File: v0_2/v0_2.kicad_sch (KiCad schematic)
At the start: 1 part, among them IC1 RASPBERRY_PI_PICO_W

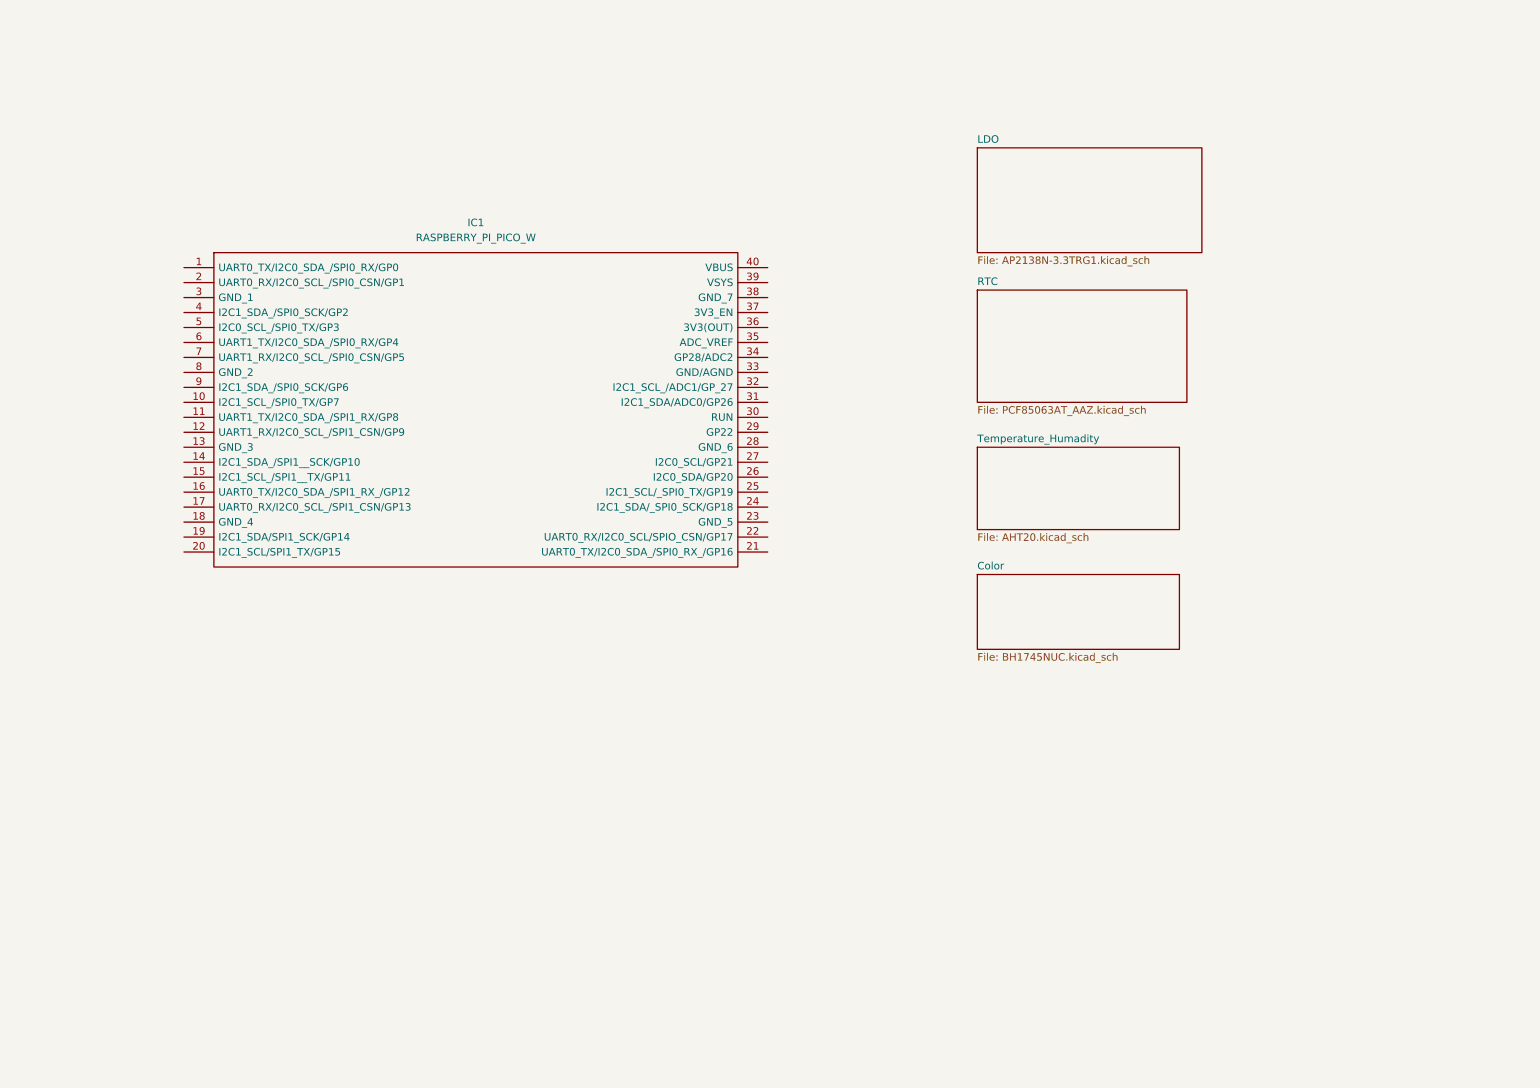
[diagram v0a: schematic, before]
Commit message: add sensor schematic
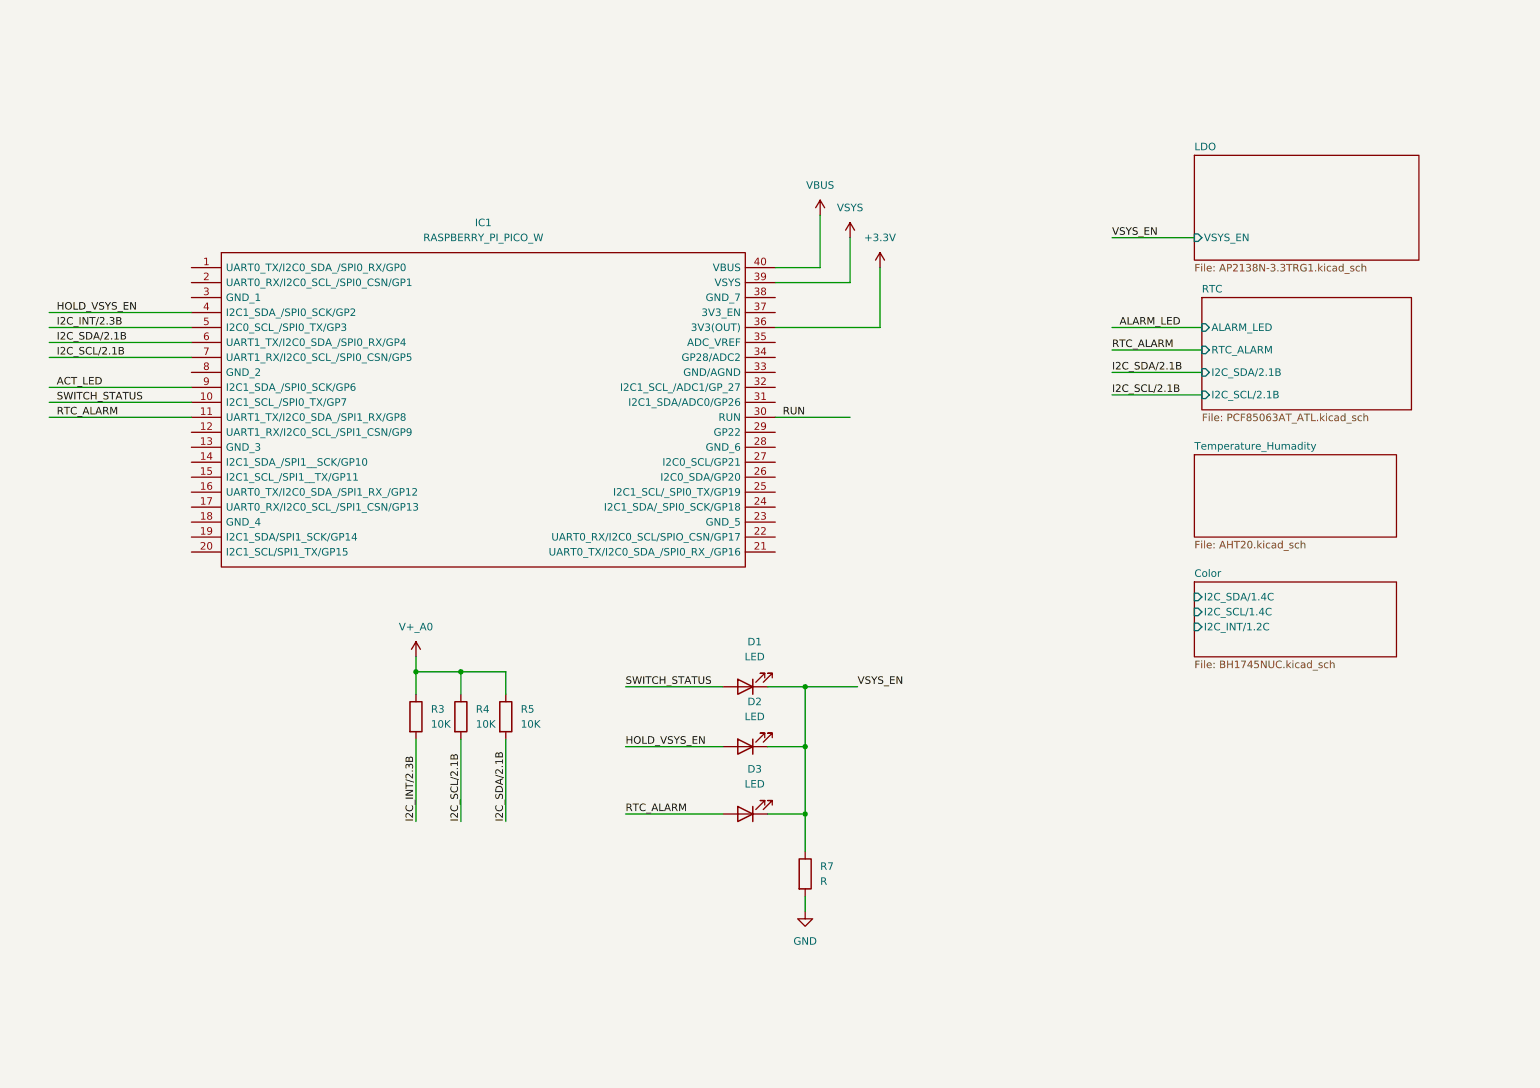
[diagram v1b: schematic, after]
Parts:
- added D1, D2, D3: LED, symbol Device:LED
- added R3, R4, R5: 10K, symbol Device:R
- added R7: R, symbol Device:R
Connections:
- net SWITCH_STATUS: now reaches IC1.10 (I2C1_SCL_/SPI0_TX/GP7)
- net SWITCH_STATUS: now also D1.2 (A)
- net RTC_ALARM: now reaches IC1.11 (UART1_TX/I2C0_SDA_/SPI1_RX/GP8)
- net RTC_ALARM: now also D3.2 (A)
- net RUN: now reaches IC1.30 (RUN)
- net +3.3V: now reaches IC1.36 (3V3(OUT))
- net VSYS: now reaches IC1.39 (VSYS)
- net HOLD_VSYS_EN: now reaches IC1.4 (I2C1_SDA_/SPI0_SCK/GP2)
- net HOLD_VSYS_EN: now also D2.2 (A)
- net VBUS: now reaches IC1.40 (VBUS)
- net I2C_INT/2.3B: now reaches IC1.5 (I2C0_SCL_/SPI0_TX/GP3)
- net I2C_INT/2.3B: now also R3.2
- net I2C_SDA/2.1B: now reaches IC1.6 (UART1_TX/I2C0_SDA_/SPI0_RX/GP4)
- net I2C_SDA/2.1B: now also R5.2
- net I2C_SCL/2.1B: now reaches IC1.7 (UART1_RX/I2C0_SCL_/SPI0_CSN/GP5)
- net I2C_SCL/2.1B: now also R4.2
- net ACT_LED: now reaches IC1.9 (I2C1_SDA_/SPI0_SCK/GP6)
- new net GND: R7.2
- new net V+_A0: R3.1, R4.1, R5.1
- new net VSYS_EN: D1.1 (K), D2.1 (K), D3.1 (K), R7.1
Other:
- sheet Color ports: added I2C_INT/1.2C, I2C_SCL/1.4C, I2C_SDA/1.4C; removed none
- sheet LDO ports: added VSYS_EN; removed none
- sheet RTC: file PCF85063AT_AAZ.kicad_sch -> PCF85063AT_ATL.kicad_sch
- sheet RTC ports: added ALARM_LED, I2C_SCL/2.1B, I2C_SDA/2.1B, RTC_ALARM; removed none
- moved on the sheet: IC1

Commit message: add color sensor
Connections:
- net RESET: now reaches IC1.12 (UART1_RX/I2C0_SCL_/SPI1_CSN/GP9)
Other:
- sheet Color: file BH1745NUC.kicad_sch -> BH1750FVI.kicad_sch
- sheet Color ports: added RESET; removed I2C_INT/1.2C
- sheet Temperature_Humadity ports: added I2C_SCL, I2C_SDA; removed none
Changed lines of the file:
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@@
+    (stroke (width 0) (type default))
+  )
+  (wire (pts (xy 204.47 115.57) (xy 218.44 115.57))
     (stroke (width 0) (type default))
   )
@@
     (stroke (width 0) (type default))
   )
+  (wire (pts (xy 204.47 99.06) (xy 218.44 99.06))
+    (stroke (width 0) (type default))
+  )
   (wire (pts (xy 121.92 140.97) (xy 138.43 140.97))
     (stroke (width 0) (type default))
@@
     (stroke (width 0) (type default))
   )
+  (wire (pts (xy 204.47 120.65) (xy 218.44 120.65))
+    (stroke (width 0) (type default))
+  )
   (wire (pts (xy 204.47 73.66) (xy 219.71 73.66))
     (stroke (width 0) (type default))
@@
     (stroke (width 0) (type default))
   )
+  (wire (pts (xy 204.47 96.52) (xy 218.44 96.52))
+    (stroke (width 0) (type default))
+  )
   (wire (pts (xy 147.32 69.85) (xy 165.1 69.85))
     (stroke (width 0) (type default))
@@
     (stroke (width 0) (type default))
   )
+  (wire (pts (xy 24.13 87.63) (xy 48.26 87.63))
+    (stroke (width 0) (type default))
+  )
   (wire (pts (xy 93.98 139.7) (xy 93.98 153.67))
     (stroke (width 0) (type default))
@@
     (stroke (width 0) (type default))
   )
+  (wire (pts (xy 204.47 118.11) (xy 218.44 118.11))
+    (stroke (width 0) (type default))
+  )
   (wire (pts (xy 165.1 69.85) (xy 165.1 59.69))
     (stroke (width 0) (type default))
@@
     (effects (font (size 1.27 1.27)) (justify left bottom))
   )
+  (label "I2C_SDA{slash}2.1B" (at 204.47 118.11 0) (fields_autoplaced)
+    (effects (font (size 1.27 1.27)) (justify left bottom))
+  )
+  (label "RESET" (at 25.4 87.63 0) (fields_autoplaced)
+    (effects (font (size 1.27 1.27)) (justify left bottom))
+  )
+  (label "RESET" (at 204.47 115.57 0) (fields_autoplaced)
+    (effects (font (size 1.27 1.27)) (justify left bottom))
+  )
   (label "HOLD_VSYS_EN" (at 25.4 67.31 0) (fields_autoplaced)
     (effects (font (size 1.27 1.27)) (justify left bottom))
@@
     (effects (font (size 1.27 1.27)) (justify left bottom))
   )
+  (label "I2C_SDA{slash}2.1B" (at 204.47 96.52 0) (fields_autoplaced)
+    (effects (font (size 1.27 1.27)) (justify left bottom))
+  )
+  (label "I2C_SCL{slash}2.1B" (at 204.47 99.06 0) (fields_autoplaced)
+    (effects (font (size 1.27 1.27)) (justify left bottom))
+  )
   (label "I2C_SCL{slash}2.1B" (at 204.47 81.28 0) (fields_autoplaced)
     (effects (font (size 1.27 1.27)) (justify left bottom))
@@
   )
   (label "I2C_INT{slash}2.3B" (at 25.4 69.85 0) (fields_autoplaced)
+    (effects (font (size 1.27 1.27)) (justify left bottom))
+  )
+  (label "I2C_SCL{slash}2.1B" (at 204.47 120.65 0) (fields_autoplaced)
     (effects (font (size 1.27 1.27)) (justify left bottom))
   )
@@
       (effects (font (size 1.27 1.27)) (justify left bottom))
     )
-    (property "Sheetfile" "BH1745NUC.kicad_sch" (at 218.44 126.3146 0)
+    (property "Sheetfile" "BH1750FVI.kicad_sch" (at 218.44 126.3146 0)
       (effects (font (size 1.27 1.27)) (justify left top))
     )
-    (pin "I2C_SDA{slash}1.4C" input (at 218.44 115.57 180)
-      (effects (font (size 1.27 1.27)) (justify left))
-    )
-    (pin "I2C_SCL{slash}1.4C" input (at 218.44 118.11 180)
-      (effects (font (size 1.27 1.27)) (justify left))
-    )
-    (pin "I2C_INT{slash}1.2C" input (at 218.44 120.65 180)
+    (pin "RESET" input (at 218.44 115.57 180)
+      (effects (font (size 1.27 1.27)) (justify left))
+    )
+    (pin "I2C_SDA{slash}1.4C" input (at 218.44 118.11 180)
+      (effects (font (size 1.27 1.27)) (justify left))
+    )
+    (pin "I2C_SCL{slash}1.4C" input (at 218.44 120.65 180)
       (effects (font (size 1.27 1.27)) (justify left))
     )
@@
       (effects (font (size 1.27 1.27)) (justify left top))
     )
-    (instances
+    (pin "I2C_SDA" input (at 218.44 96.52 180)
+      (effects (font (size 1.27 1.27)) (justify left))
+    )
+    (pin "I2C_SCL" input (at 218.44 99.06 180)
+      (effects (font (size 1.27 1.27)) (justify left))
+    )
+    (instances

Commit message: schematic for enviro done
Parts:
- removed D3: LED, symbol Device:LED
- added D3: 1PS88SB48, Package_TO_SOT_SMD:SOT-363_SC-70-6, symbol PCM_Diode_Schottky_AKL:1PS88SB48
- added R15, R16: R, symbol Device:R
- added S1, S2: TS-1101-C-W, TS-1101-C-W:TS1101CW, symbol TS-1101-C-W:TS-1101-C-W
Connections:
- net +3.3V: now also R3.1, R4.1, R5.1
- net ACT_LED: now also R7.1
- net ALARM_LED: now also R15.1
- net GND: now also D1.1 (K), D2.1 (K), R16.2, S1.2 (NO); no longer R7.2
- net HOLD_VSYS_EN: now also D3.4 (A2); no longer D2.2 (A)
- net RTC_ALARM: now also D3.5 (A2)
- net RUN: now also S1.1 (COM)
- net SWITCH_STATUS: now also D3.1 (A1), S2.1 (COM); no longer D1.2 (A)
- net V+_A0: now also S2.2 (NO); no longer R3.1, R4.1, R5.1
- net VSYS_EN: now also D3.3 (K2), D3.6 (K1), R16.1; no longer D1.1 (K), D2.1 (K), R7.1
- new net: D2.2 (A), R15.2
- new net: D1.2 (A), R7.2
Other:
- sheet LDO ports: added V+_A0; removed none
- sheet RTC ports: added V+_A0; removed none
- note added: "User Interface"
- moved on the sheet: D1, D2, R3, R4, R5

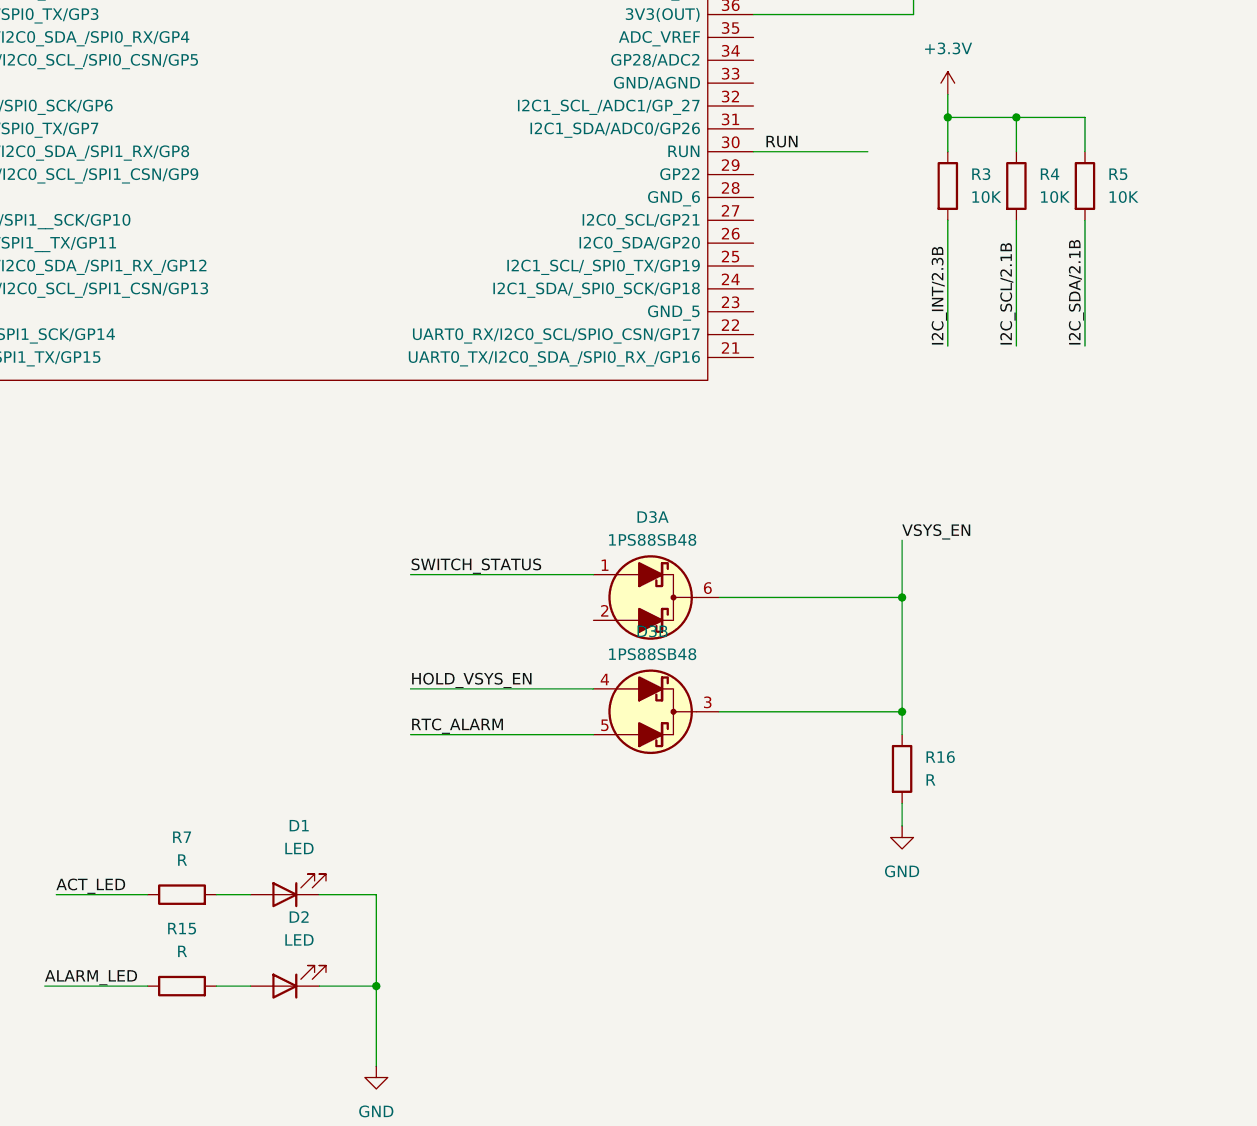
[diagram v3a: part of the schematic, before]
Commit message: all part are added
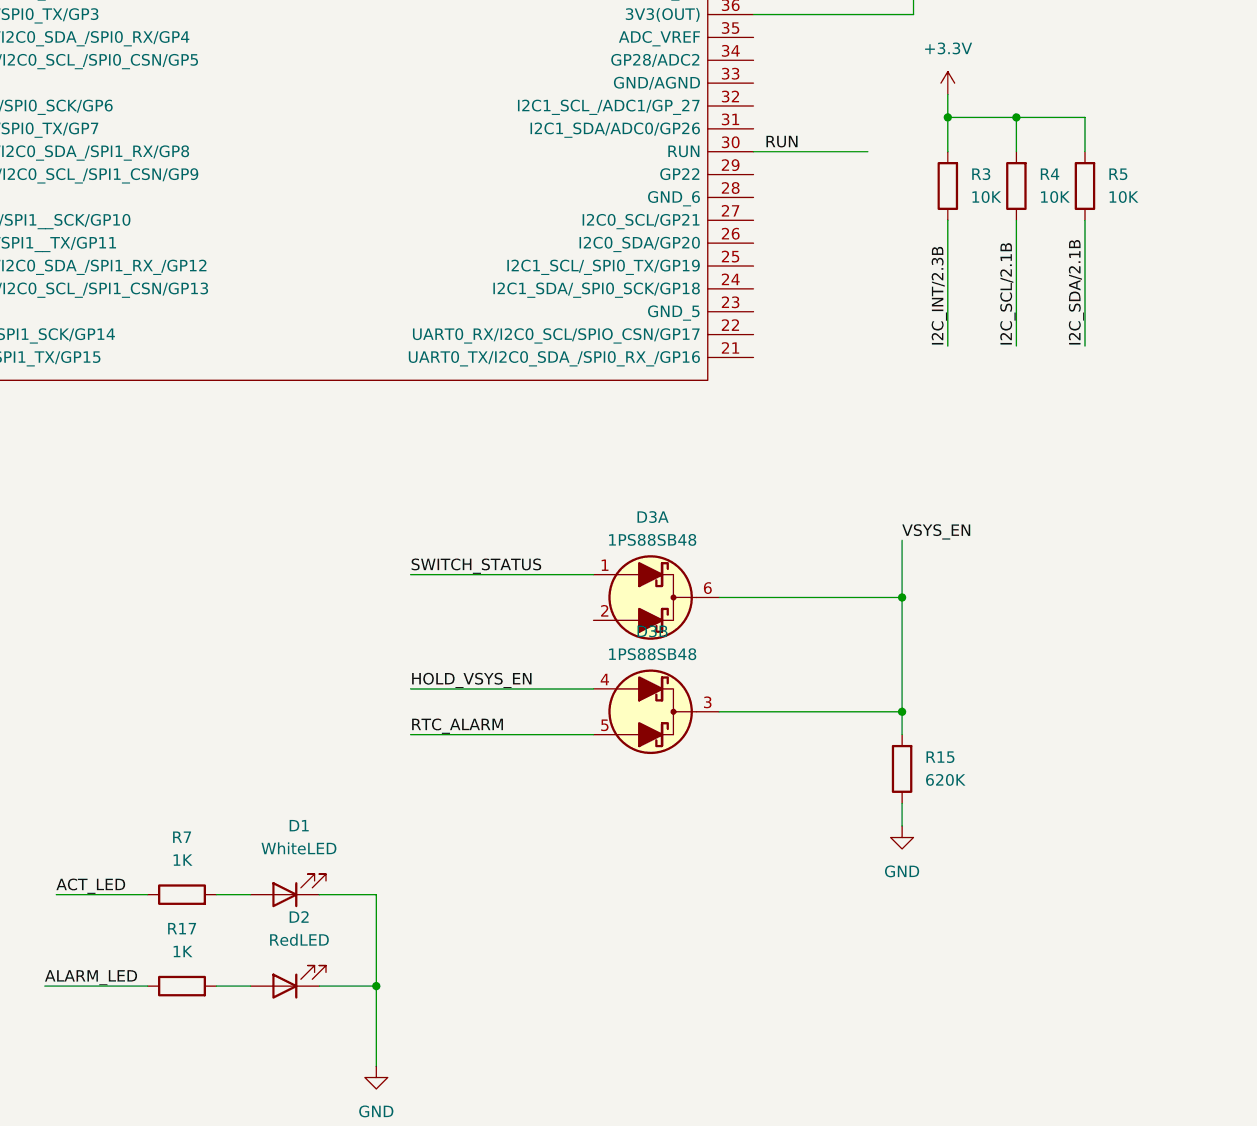
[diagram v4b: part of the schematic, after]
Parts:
- removed R16: R, symbol Device:R
- added R17: 1K, Resistor_SMD:R_0603_1608Metric, symbol Device:R
- D1: value LED -> WhiteLED; footprint (none) -> LED_SMD:LED_0603_1608Metric; Manufacturer_Part_Number (none) -> SML-E12V8WT86
- D2: value LED -> RedLED; footprint (none) -> LED_SMD:LED_0603_1608Metric; Manufacturer_Part_Number (none) -> XL-1608VRC-06
- R15: value R -> 620K; footprint (none) -> Resistor_SMD:R_0603_1608Metric; Manufacturer_Part_Number (none) -> 0603WAF6203T5E
- R3, R4, R5: footprint (none) -> Resistor_SMD:R_0603_1608Metric; Manufacturer_Part_Number (none) -> 0603WAF1002T5E
- R7: value R -> 1K; footprint (none) -> Resistor_SMD:R_0603_1608Metric; Manufacturer_Part_Number (none) -> 0603WAF1001T5E
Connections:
- net +3.3V: now also R3.2, R4.2, R5.2; no longer R3.1, R4.1, R5.1
- net ALARM_LED: now also R17.1; no longer R15.1
- net GND: now also R15.1
- net I2C_INT/2.3B: now also R3.1; no longer R3.2
- net I2C_SCL/2.1B: now also R4.1; no longer R4.2
- net I2C_SDA/2.1B: now also R5.1; no longer R5.2
- net VSYS_EN: now also R15.2
- net at D2.2 (A): now also R17.2; no longer R15.2
